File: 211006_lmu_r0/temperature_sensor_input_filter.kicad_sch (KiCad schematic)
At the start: 3 parts

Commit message: merge PCB
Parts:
- renumbered C17 to C24, R6 to R20, R7 to R21
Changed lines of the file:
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@@
   (symbol (lib_id "Device:R") (at 167.64 91.44 270)
     (in_bom yes) (on_board yes)
-    (property "Reference" "R7" (id 0) (at 167.64 86.1822 90))
+    (property "Reference" "R21" (id 0) (at 167.64 86.1822 90))
     (property "Value" "50kR" (id 1) (at 167.64 88.4936 90))
     (property "Footprint" "Resistor_SMD:R_0603_1608Metric_Pad0.98x0.95mm_HandSolder" (id 2) (at 167.64 89.662 90)
@@
   (symbol (lib_id "Device:C") (at 158.75 97.79 180)
     (in_bom yes) (on_board yes)
-    (property "Reference" "C17" (id 0) (at 161.671 96.6216 0)
+    (property "Reference" "C24" (id 0) (at 161.671 96.6216 0)
       (effects (font (size 1.27 1.27)) (justify right))
     )
@@
   (symbol (lib_id "Device:R") (at 158.75 85.09 180)
     (in_bom yes) (on_board yes)
-    (property "Reference" "R6" (id 0) (at 162.56 82.55 0))
+    (property "Reference" "R20" (id 0) (at 162.56 82.55 0))
     (property "Value" "10kR" (id 1) (at 162.56 85.09 0))
     (property "Footprint" "Resistor_SMD:R_0603_1608Metric_Pad0.98x0.95mm_HandSolder" (id 2) (at 160.528 85.09 90)
@@
   (symbol (lib_id "gnd_hv:GND_HV") (at 158.75 101.6 0)
     (in_bom yes) (on_board yes) (fields_autoplaced)
-    (property "Reference" "#PWR0120" (id 0) (at 158.75 107.95 0)
+    (property "Reference" "#PWR0141" (id 0) (at 158.75 107.95 0)
       (effects (font (size 1.27 1.27)) hide)
     )
@@
   (symbol (lib_id "+5v_hv:+5V_HV") (at 158.75 81.28 0)
     (in_bom yes) (on_board yes) (fields_autoplaced)
-    (property "Reference" "#PWR0119" (id 0) (at 158.75 85.09 0)
+    (property "Reference" "#PWR0140" (id 0) (at 158.75 85.09 0)
       (effects (font (size 1.27 1.27)) hide)
     )

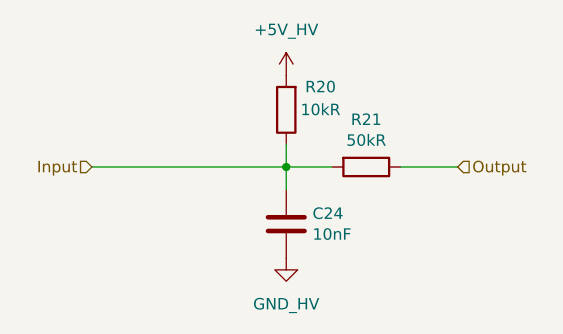
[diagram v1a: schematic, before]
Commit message: Lots of routing and placing, according to planned layout
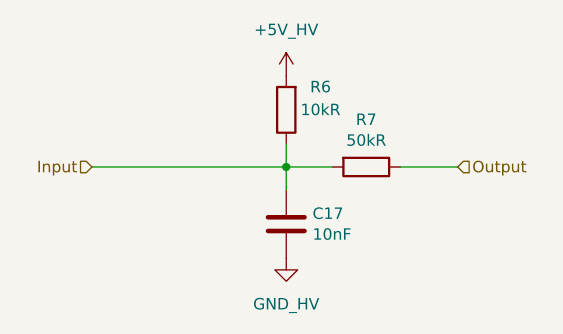
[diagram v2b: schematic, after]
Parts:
- renumbered C24 to C17, R20 to R6, R21 to R7
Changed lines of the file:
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@@
   (symbol (lib_id "Device:R") (at 167.64 91.44 270)
     (in_bom yes) (on_board yes)
-    (property "Reference" "R21" (id 0) (at 167.64 86.1822 90))
+    (property "Reference" "R7" (id 0) (at 167.64 86.1822 90))
     (property "Value" "50kR" (id 1) (at 167.64 88.4936 90))
     (property "Footprint" "Resistor_SMD:R_0603_1608Metric_Pad0.98x0.95mm_HandSolder" (id 2) (at 167.64 89.662 90)
@@
   (symbol (lib_id "Device:C") (at 158.75 97.79 180)
     (in_bom yes) (on_board yes)
-    (property "Reference" "C24" (id 0) (at 161.671 96.6216 0)
+    (property "Reference" "C17" (id 0) (at 161.671 96.6216 0)
       (effects (font (size 1.27 1.27)) (justify right))
     )
@@
   (symbol (lib_id "Device:R") (at 158.75 85.09 180)
     (in_bom yes) (on_board yes)
-    (property "Reference" "R20" (id 0) (at 162.56 82.55 0))
+    (property "Reference" "R6" (id 0) (at 162.56 82.55 0))
     (property "Value" "10kR" (id 1) (at 162.56 85.09 0))
     (property "Footprint" "Resistor_SMD:R_0603_1608Metric_Pad0.98x0.95mm_HandSolder" (id 2) (at 160.528 85.09 90)
